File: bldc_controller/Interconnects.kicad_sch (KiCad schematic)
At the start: 46 parts, among them J10 B2B-PH-K-S (LF)(SN), J3 SM08B-GHS-TB, J4 SM07B-GHS-TB, J5 01x02 2.54mm Pads, J6 SM06B-GHS-TB, J7 Microfit 3.0 1x03, J8 Microfit 3.0 1x03, J9 SWD_02x05_1.27mm, SW1 CAS-220TA

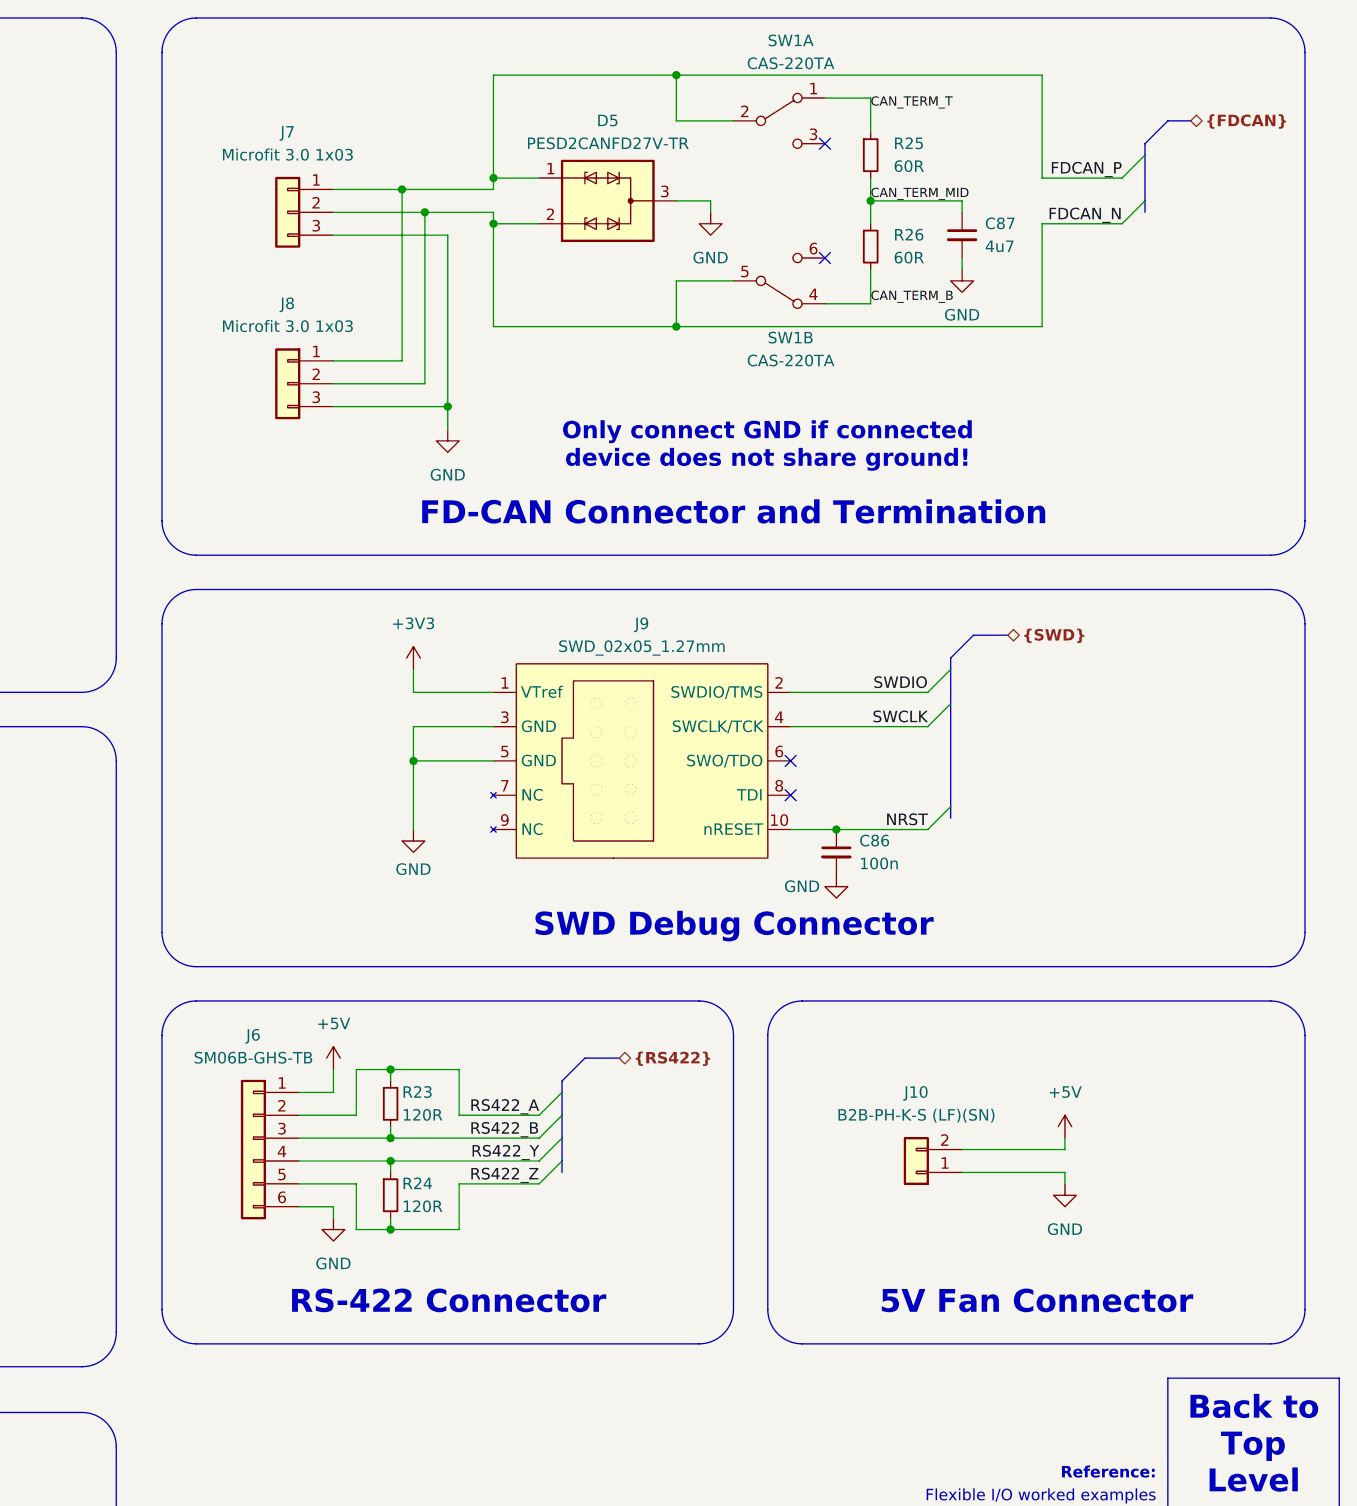
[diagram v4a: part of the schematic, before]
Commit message: routed CAN, added new footprints
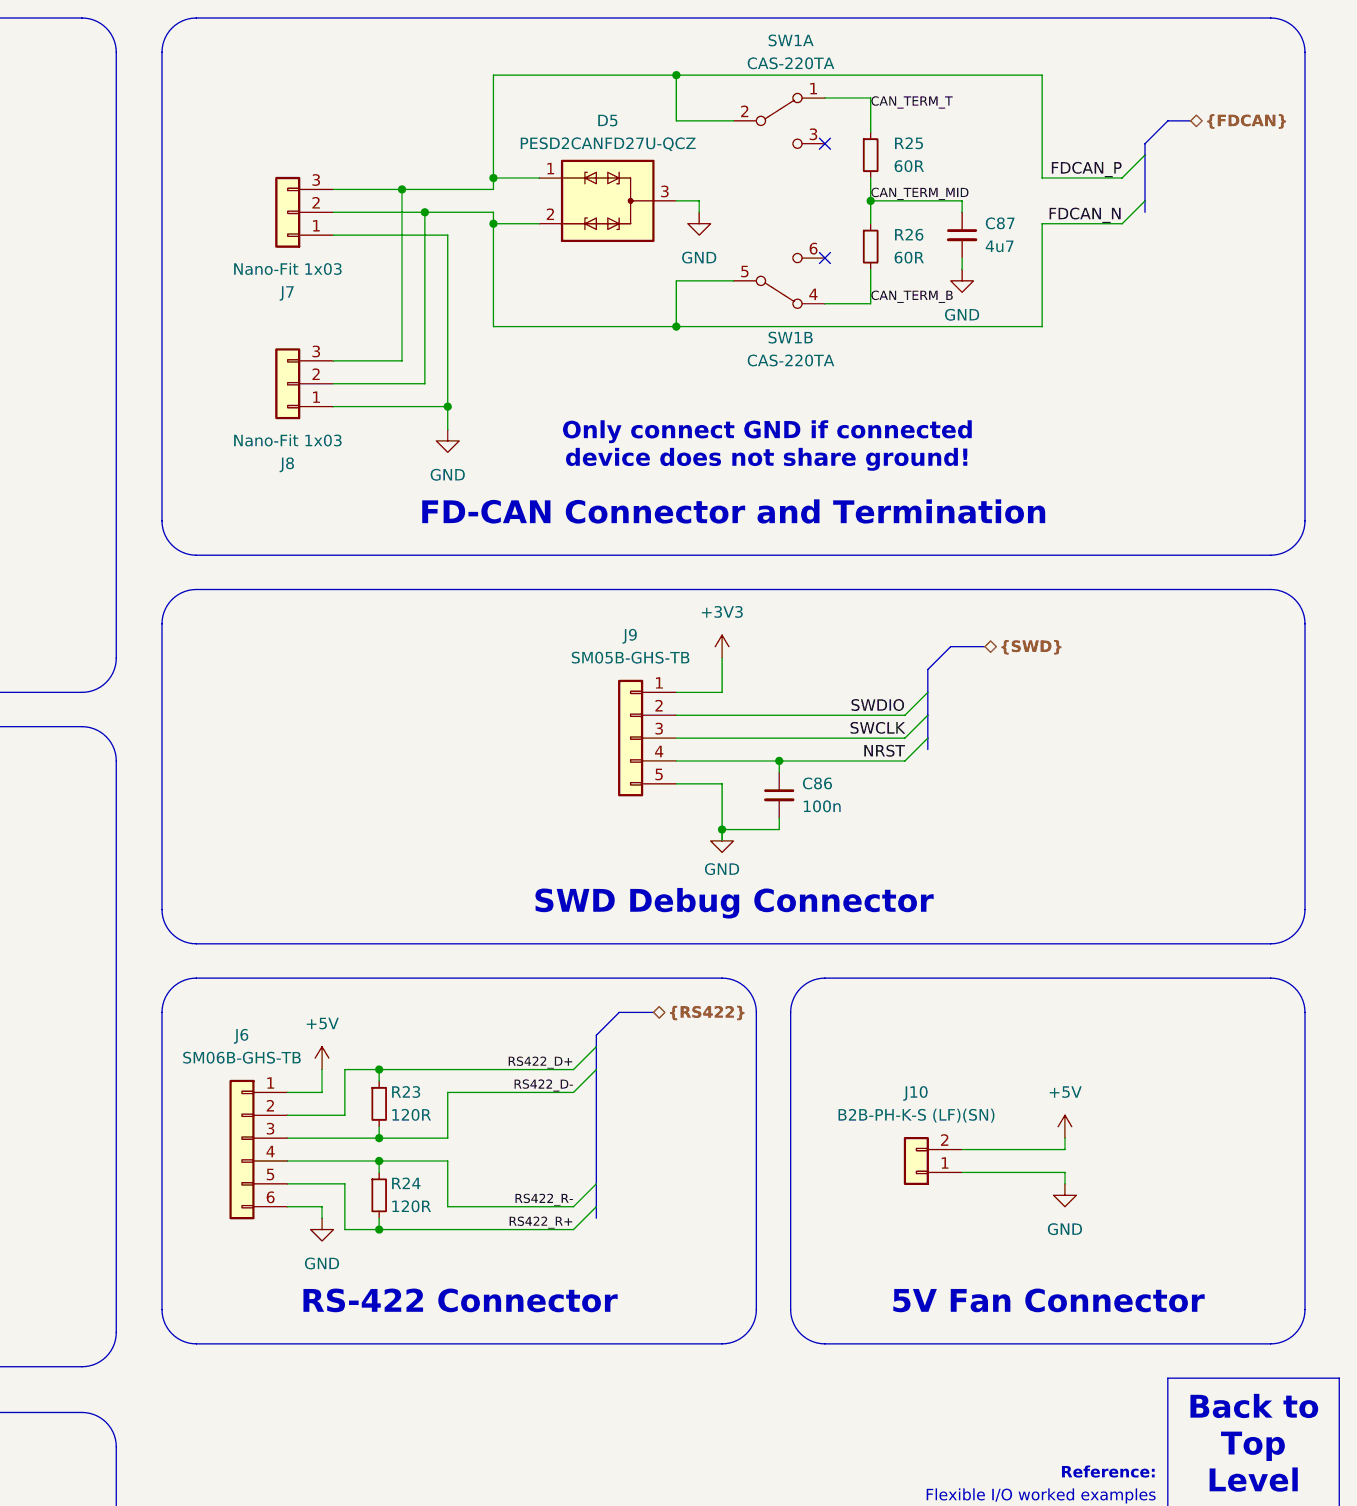
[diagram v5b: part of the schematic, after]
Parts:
- removed D5: PESD2CANFD27V-TR, Package_TO_SOT_SMD:SOT-23, symbol 0_power_protection:PESD2CANFD27V-TR
- removed J9: SWD_02x05_1.27mm, 0_connectors:3220-10-0200-00, symbol 0_connectors:SWD_02x05_1.27mm
- added D5: PESD2CANFD27U-QCZ, 0_package_SOT_TO_SMD:SOT8009, symbol 0_power_protection:PESD2CANFD27U-QCZ
- added J9: SM05B-GHS-TB, Connector_JST:JST_GH_SM05B-GHS-TB_1x05-1MP_P1.25mm_Horizontal, symbol Connector_Generic:Conn_01x05
- C87: footprint 0_capacitor_smd:C_0603_1608_DensityHigh -> 0_capacitor_smd:C_0402_1005_DensityHigh
- J7, J8: value Microfit 3.0 1x03 -> Nano-Fit 1x03; footprint Connector_Molex:Molex_Micro-Fit_3.0_43650-0310_1x03-1MP_P3.00mm_Horizontal -> 0_connectors:1054301203
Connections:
- net +3V3: now also J9.1 (Pin_1)
- net FDCAN_N: now also D5.2 (K2)
- net FDCAN_P: now also J7.3 (Pin_3), J8.3 (Pin_3), D5.1 (K1); no longer J7.1 (Pin_1), J8.1 (Pin_1)
- net GND: now also J7.1 (Pin_1), J8.1 (Pin_1), D5.3 (CC), J9.5 (Pin_5); no longer J7.3 (Pin_3), J8.3 (Pin_3)
- net NRST: now also J9.4 (Pin_4)
- net SWCLK: now also J9.3 (Pin_3)
- net SWDIO: now also J9.2 (Pin_2)
- net RS422_A renamed RS422_D+
- net RS422_B renamed RS422_D-
- net RS422_Y renamed RS422_R-
- net RS422_Z renamed RS422_R+
- no-connect marks 4 -> 2
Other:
- moved on the sheet: C86, J6, J7, J8, R23, R24

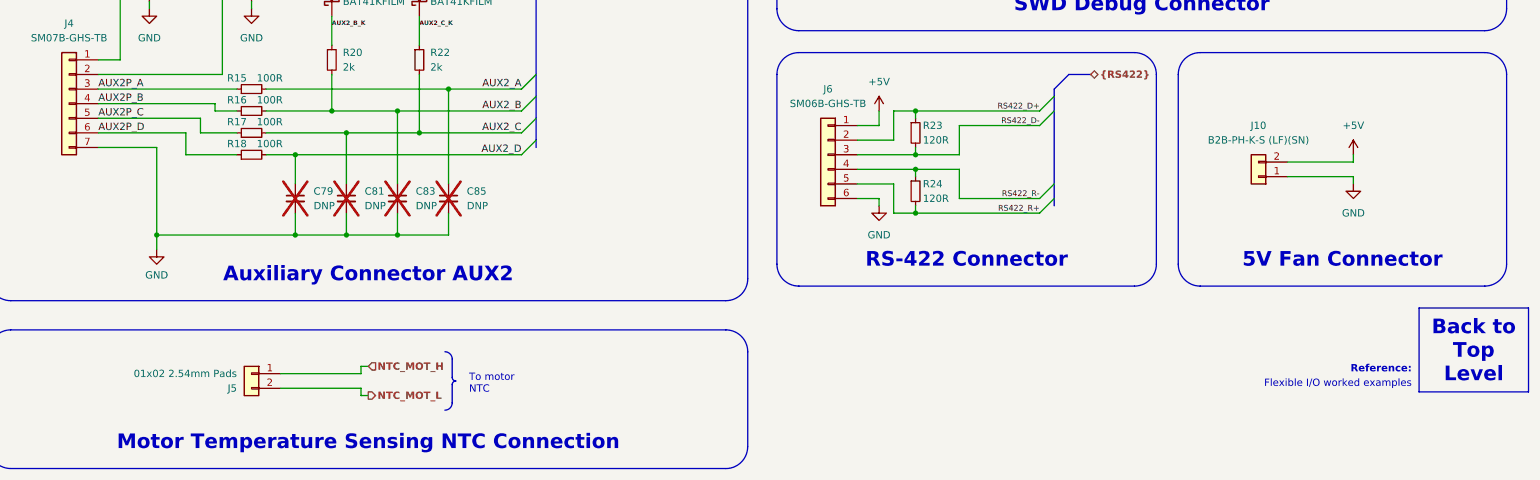
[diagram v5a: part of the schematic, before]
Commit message: added power domains. Risk of ground shift near CAN
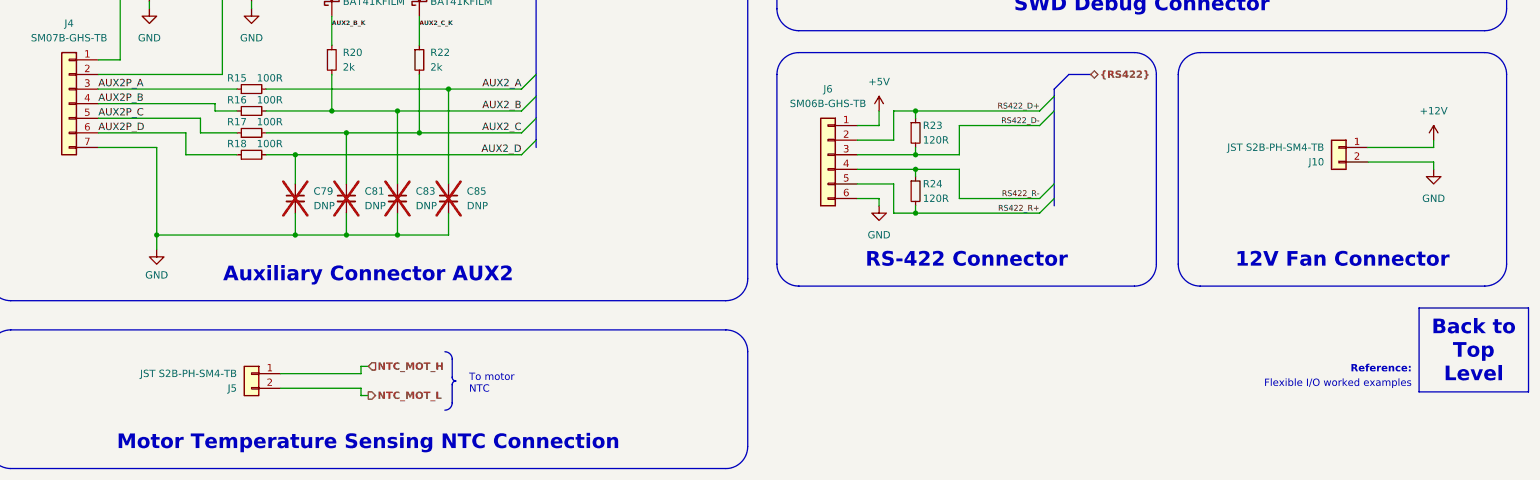
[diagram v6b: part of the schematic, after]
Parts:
- J10: value B2B-PH-K-S (LF)(SN) -> JST S2B-PH-SM4-TB; footprint Connector_JST:JST_PH_B2B-PH-K_1x02_P2.00mm_Vertical -> Connector_JST:JST_PH_S2B-PH-SM4-TB_1x02-1MP_P2.00mm_Horizontal
- J5: value 01x02 2.54mm Pads -> JST S2B-PH-SM4-TB; footprint Connector_PinHeader_2.54mm:PinHeader_1x02_P2.54mm_Vertical -> Connector_JST:JST_PH_S2B-PH-SM4-TB_1x02-1MP_P2.00mm_Horizontal
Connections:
- net +5V: no longer J10.2 (Pin_2)
- net GND: now also J10.2 (Pin_2); no longer J10.1 (Pin_1)
- new net +12V: J10.1 (Pin_1)
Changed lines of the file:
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@@
     (stroke (width 0) (type default))
   )
-  (wire (pts (xy 254 140.97) (xy 242.57 140.97))
+  (wire (pts (xy 267.97 138.43) (xy 256.54 138.43))
     (stroke (width 0) (type default))
   )
@@
     (stroke (width 0) (type default))
   )
-  (wire (pts (xy 254 139.7) (xy 254 140.97))
+  (wire (pts (xy 267.97 137.16) (xy 267.97 138.43))
     (stroke (width 0) (type default))
   )
@@
     (stroke (width 0) (type default))
   )
-  (wire (pts (xy 254 144.78) (xy 254 143.51))
+  (wire (pts (xy 267.97 142.24) (xy 267.97 140.97))
     (stroke (width 0) (type default))
   )
@@
     (stroke (width 0) (type default))
   )
-  (wire (pts (xy 254 143.51) (xy 242.57 143.51))
+  (wire (pts (xy 267.97 140.97) (xy 256.54 140.97))
     (stroke (width 0) (type default))
   )
@@
     (effects (font (size 2.54 2.54) (thickness 0.508) bold (color 0 0 0 1)) (justify bottom))
   )
-  (text_box "5V Fan Connector"
+  (text_box "12V Fan Connector"
     (at 223.52 153.67 0) (size 57.15 7.62)
     (stroke (width -0.0001) (type default))
@@
     )
   )
-  (symbol (lib_id "power:GND") (at 254 144.78 0) (unit 1)
-    (in_bom yes) (on_board yes) (dnp no) (fields_autoplaced)
-    (property "Reference" "#PWR043" (at 254 151.13 0)
-      (effects (font (size 1.27 1.27)) hide)
-    )
-    (property "Value" "GND" (at 254 149.86 0)
-      (effects (font (size 1.27 1.27)))
-    )
-    (property "Footprint" "" (at 254 144.78 0)
-      (effects (font (size 1.27 1.27)) hide)
-    )
-    (property "Datasheet" "" (at 254 144.78 0)
+  (symbol (lib_id "power:GND") (at 267.97 142.24 0) (unit 1)
+    (in_bom yes) (on_board yes) (dnp no) (fields_autoplaced)
+    (property "Reference" "#PWR043" (at 267.97 148.59 0)
+      (effects (font (size 1.27 1.27)) hide)
+    )
+    (property "Value" "GND" (at 267.97 147.32 0)
+      (effects (font (size 1.27 1.27)))
+    )
+    (property "Footprint" "" (at 267.97 142.24 0)
+      (effects (font (size 1.27 1.27)) hide)
+    )
+    (property "Datasheet" "" (at 267.97 142.24 0)
       (effects (font (size 1.27 1.27)) hide)
     )
@@
     )
   )
-  (symbol (lib_id "Connector_Generic:Conn_01x02") (at 237.49 143.51 180) (unit 1)
-    (in_bom yes) (on_board yes) (dnp no) (fields_autoplaced)
-    (property "Reference" "J10" (at 237.49 134.62 0)
-      (effects (font (size 1.27 1.27)))
-    )
-    (property "Value" "B2B-PH-K-S (LF)(SN)" (at 237.49 137.16 0)
-      (effects (font (size 1.27 1.27)))
-    )
-    (property "Footprint" "Connector_JST:JST_PH_B2B-PH-K_1x02_P2.00mm_Vertical" (at 237.49 143.51 0)
-      (effects (font (size 1.27 1.27)) hide)
-    )
-    (property "Datasheet" "~" (at 237.49 143.51 0)
-      (effects (font (size 1.27 1.27)) hide)
-    )
-    (pin "1")
-    (pin "2")
-    (instances
-      (project "bldc_controller"
-        (path "/0650c7a8-acba-429c-9f8e-eec0baf0bc1c/e3d7d553-09c9-41e5-aeb8-81d1255a4873"
-          (reference "J10") (unit 1)
-        )
-      )
-    )
-  )
   (symbol (lib_id "power:GND") (at 215.9 105.41 0) (unit 1)
     (in_bom yes) (on_board yes) (dnp no) (fields_autoplaced)
@@
     )
   )
-  (symbol (lib_id "power:+5V") (at 254 139.7 0) (unit 1)
-    (in_bom yes) (on_board yes) (dnp no) (fields_autoplaced)
-    (property "Reference" "#PWR042" (at 254 143.51 0)
-      (effects (font (size 1.27 1.27)) hide)
-    )
-    (property "Value" "+5V" (at 254 134.62 0)
-      (effects (font (size 1.27 1.27)))
-    )
-    (property "Footprint" "" (at 254 139.7 0)
-      (effects (font (size 1.27 1.27)) hide)
-    )
-    (property "Datasheet" "" (at 254 139.7 0)
-      (effects (font (size 1.27 1.27)) hide)
-    )
-    (pin "1")
-    (instances
-      (project "bldc_controller"
-        (path "/0650c7a8-acba-429c-9f8e-eec0baf0bc1c/e3d7d553-09c9-41e5-aeb8-81d1255a4873"
-          (reference "#PWR042") (unit 1)
-        )
-      )
-    )
-  )
   (symbol (lib_id "Device:C_Small") (at 87.63 147.32 0) (unit 1)
     (in_bom no) (on_board yes) (dnp yes) (fields_autoplaced)
@@
     )
   )
+  (symbol (lib_id "power:+12V") (at 267.97 137.16 0) (unit 1)
+    (in_bom yes) (on_board yes) (dnp no) (fields_autoplaced)
+    (property "Reference" "#PWR042" (at 267.97 140.97 0)
+      (effects (font (size 1.27 1.27)) hide)
+    )
+    (property "Value" "+12V" (at 267.97 132.08 0)
+      (effects (font (size 1.27 1.27)))
+    )
+    (property "Footprint" "" (at 267.97 137.16 0)
+      (effects (font (size 1.27 1.27)) hide)
+    )
+    (property "Datasheet" "" (at 267.97 137.16 0)
+      (effects (font (size 1.27 1.27)) hide)
+    )
+    (pin "1")
+    (instances
+      (project "bldc_controller"
+        (path "/0650c7a8-acba-429c-9f8e-eec0baf0bc1c/e3d7d553-09c9-41e5-aeb8-81d1255a4873"
+          (reference "#PWR042") (unit 1)
+        )
+      )
+    )
+  )
   (symbol (lib_id "Device:C_Small") (at 96.52 73.66 0) (unit 1)
     (in_bom no) (on_board yes) (dnp yes) (fields_autoplaced)
@@
       (effects (font (size 1.27 1.27)) (justify left))
     )
-    (property "Value" "01x02 2.54mm Pads" (at 59.69 177.8 0)
-      (effects (font (size 1.27 1.27)) (justify left))
-    )
-    (property "Footprint" "Connector_PinHeader_2.54mm:PinHeader_1x02_P2.54mm_Vertical" (at 62.23 177.8 0)
+    (property "Value" "JST S2B-PH-SM4-TB" (at 59.69 177.8 0)
+      (effects (font (size 1.27 1.27)) (justify left))
+    )
+    (property "Footprint" "Connector_JST:JST_PH_S2B-PH-SM4-TB_1x02-1MP_P2.00mm_Horizontal" (at 62.23 177.8 0)
       (effects (font (size 1.27 1.27)) hide)
     )
@@
         )
       )
+    )
+  )
+  (symbol (lib_id "Connector_Generic:Conn_01x02") (at 251.46 138.43 0) (mirror y) (unit 1)
+    (in_bom yes) (on_board yes) (dnp no)
+    (property "Reference" "J10" (at 248.92 140.97 0)
+      (effects (font (size 1.27 1.27)) (justify left))
+    )
+    (property "Value" "JST S2B-PH-SM4-TB" (at 248.92 138.43 0)
+      (effects (font (size 1.27 1.27)) (justify left))
+    )
+    (property "Footprint" "Connector_JST:JST_PH_S2B-PH-SM4-TB_1x02-1MP_P2.00mm_Horizontal" (at 251.46 138.43 0)
+      (effects (font (size 1.27 1.27)) hide)
+    )
+    (property "Datasheet" "~" (at 251.46 138.43 0)
+      (effects (font (size 1.27 1.27)) hide)
+    )
+    (pin "1")
+    (pin "2")
+    (instances
+      (project "bldc_controller"
+        (path "/0650c7a8-acba-429c-9f8e-eec0baf0bc1c/e3d7d553-09c9-41e5-aeb8-81d1255a4873"
+          (reference "J10") (unit 1)
+        )
+      )

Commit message: Added TVS diodes to all interfaces
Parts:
- removed D5: PESD2CANFD27U-QCZ, 0_package_SOT_TO_SMD:SOT8009, symbol 0_power_protection:PESD2CANFD27U-QCZ
- added D17, D5: PESD2CANFD24V-UX, Package_TO_SOT_SMD:SOT-323_SC-70, symbol 0_power_protection:PESD2CANFD24V-UX
- added D18, D19: CDSOT23-SM712, Package_TO_SOT_SMD:SOT-23, symbol 0_power_protection:CDSOT23-SM712
- added D20, D21: PESD4USB5B-TTSX, 0_package_DFN_QFN:DFN2510-D10, symbol 0_power_protection:PESD4USB5B-TTSX
- added D22, D23: PESD4USB3U-TTSX, 0_package_DFN_QFN:DFN2510-D10, symbol 0_power_protection:PESD4USB5B-TTSX_1
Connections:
- net AUX1P_A: now also D22.5 (K), D22.6 (K)
- net AUX1P_B: now also D22.4 (K), D22.7 (K)
- net AUX1P_C: now also D22.1 (K), D22.10 (K)
- net AUX1P_D: now also D21.5 (K), D21.6 (K)
- net AUX1P_E: now also D21.1 (K), D21.10 (K)
- net AUX2P_A: now also D20.5 (K), D20.6 (K)
- net AUX2P_B: now also D20.4 (K), D20.7 (K)
- net AUX2P_C: now also D20.2 (K), D20.9 (K)
- net AUX2P_D: now also D20.1 (K), D20.10 (K)
- net FDCAN_N: now also J7.3 (Pin_3), J8.3 (Pin_3), SW1.2 (B), D17.1 (K1), D5.1 (K1); no longer J7.2 (Pin_2), J8.2 (Pin_2), SW1.5 (B)
- net FDCAN_P: now also J7.2 (Pin_2), J8.2 (Pin_2), SW1.5 (B), D17.2 (K2), D5.2 (K2); no longer J7.3 (Pin_3), J8.3 (Pin_3), SW1.2 (B)
- net GND: now also D17.3 (CC), D18.3 (common), D19.3 (common), D20.3 (A), D20.8 (A), D21.3 (A), D21.8 (A), D22.3 (A), D22.8 (A), D23.3 (A), D23.8 (A), D5.3 (CC); no longer J10.2 (Pin_2)
- net NRST: now also D23.1 (K), D23.10 (K)
- net RS422_D+: now also J6.5 (Pin_5), R24.2, D18.2 (A2); no longer J6.2 (Pin_2), R23.1
- net RS422_D-: now also J6.4 (Pin_4), R24.1, D18.1 (A1); no longer J6.3 (Pin_3), R23.2
- net RS422_R+: now also J6.2 (Pin_2), R23.1, D19.1 (A1); no longer J6.5 (Pin_5), R24.2
- net RS422_R-: now also J6.3 (Pin_3), R23.2, D19.2 (A2); no longer J6.4 (Pin_4), R24.1
- net SWCLK: now also D23.4 (K), D23.7 (K)
- net SWDIO: now also D23.5 (K), D23.6 (K)
- new net: D23.2 (K), D23.9 (K)
- new net: D22.2 (K), D22.9 (K)
- new net: D21.2 (K), D21.9 (K)
- new net: D21.4 (K), D21.7 (K)
- new net FAN_SW: J10.2 (Pin_2)
- no-connect marks 2 -> 6
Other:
- moved on the sheet: C76, C78, C79, C80, C81, C82, C83, C84, C85, C86, C87, D?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
